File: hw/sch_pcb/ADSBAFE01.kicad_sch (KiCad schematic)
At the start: 66 parts, among them J1 HEADER_2x02_PARALLEL, J2 HEADER_2x12_PARALLEL, J3 MCX 6GHz 50R, M1 HOLE, M2 HOLE, M3 HOLE, M4 HOLE, M5 RFShield_TwoPieces, SW1 SN74LVC1G3157, SW2 SN74LVC1G3157, U1 BGA2818, U2 AD8313xRM, U3 TLV3542, U4 MCP4017-104E 100k, U5 MCP6566, X1 SF2321D

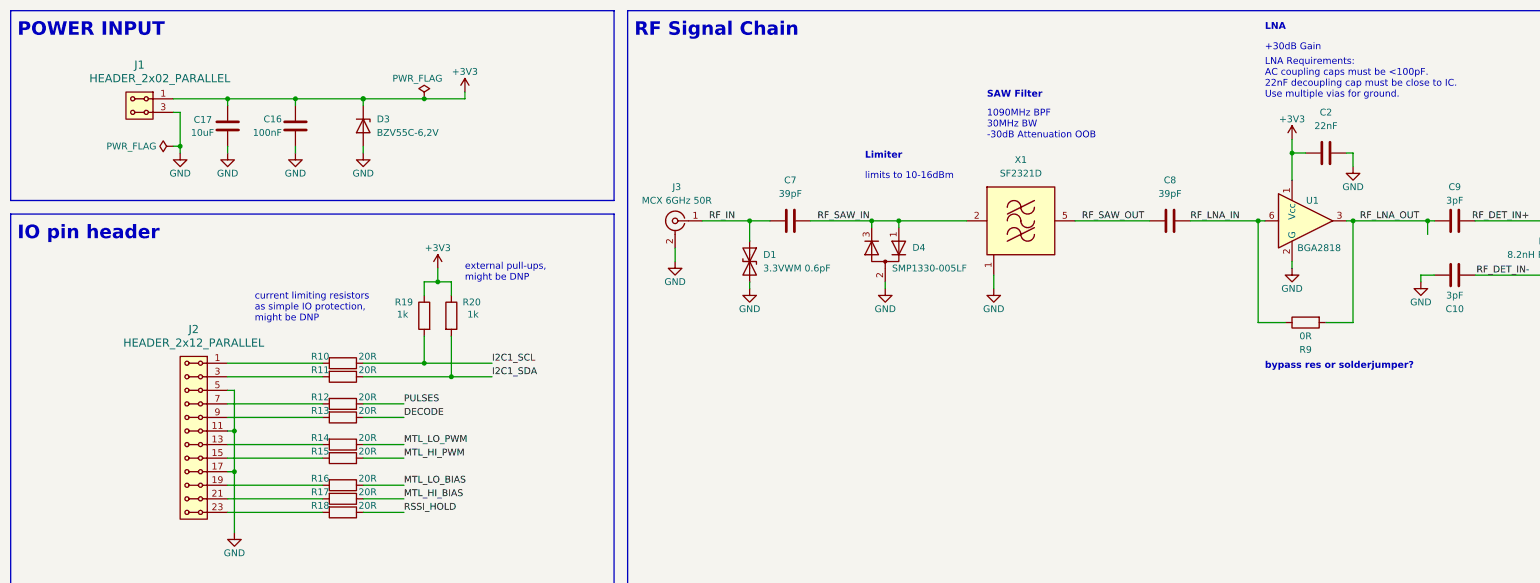
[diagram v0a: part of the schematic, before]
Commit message: first draft of layout
Parts placement viable. Traces sketched only to test whether connections
are viable.
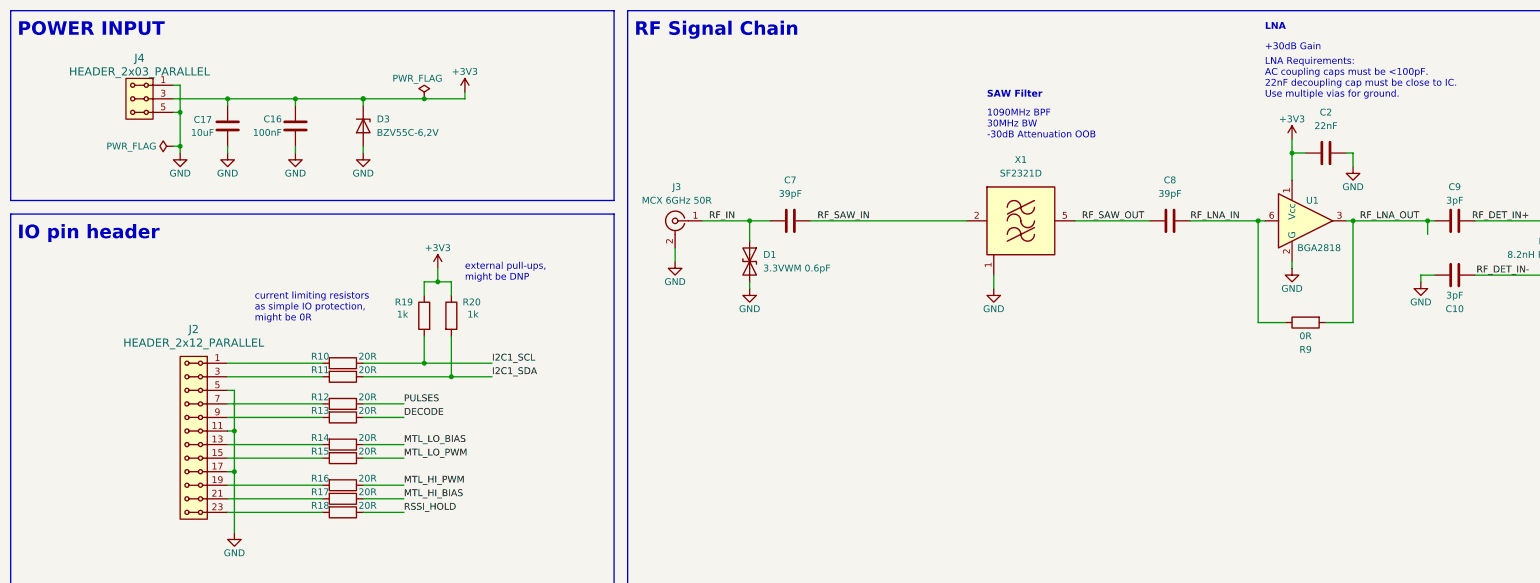
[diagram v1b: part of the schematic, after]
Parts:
- removed D4: SMP1330-005LF, Package_TO_SOT_SMD:SOT-23_Handsoldering, symbol Device:D_Dual_Series_ACK_Parallel
- removed J1: HEADER_2x02_PARALLEL, Mlab_Pin_Headers:Straight_2x02, symbol MLAB_HEADER:HEADER_2x02_PARALLEL
- added J4: HEADER_2x03_PARALLEL, Mlab_Pin_Headers:Straight_2x03, symbol MLAB_HEADER:HEADER_2x03_PARALLEL
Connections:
- net +3V3: now also J4.3, J4.4
- net GND: now also J4.1, J4.2, J4.5, J4.6
- net MTL_HI_PWM: now also R16.1; no longer R15.1
- net MTL_LO_BIAS: now also R14.1; no longer R16.1
- net MTL_LO_PWM: now also R15.1; no longer R14.1
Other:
- note added: "current limiting resistors as simple IO protection, might be 0R"
- note removed: "Limiter"
- note removed: "bypass res or solderjumper?"
- note removed: "current limiting resistors as simple IO protection, might be DNP"
- note removed: "limits to 10-16dBm"

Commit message: Layout done, silk WIP
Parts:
- removed TP1, TP4, TP6, TP7, TP8: TestPoint, TestPoint:TestPoint_Pad_D1.0mm, symbol Connector:TestPoint
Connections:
- net GND: now also J2.19, J2.20; no longer J2.17, J2.18
- net at J2.10, J2.9: now also R17.2; no longer R13.2
- net at J2.23, J2.24: now also R11.2; no longer R18.2
- net at J2.7, J2.8: now also R16.2; no longer R12.2
- net at J2.1, J2.2: now also R14.2; no longer R10.2
- net at J2.15, J2.16: now also R13.2; no longer R15.2
- net at J2.21, J2.22: now also R10.2; no longer R17.2
- net at J2.13, J2.14: now also R12.2; no longer R14.2
- net at J2.3, J2.4: now also R15.2; no longer R11.2
- new net: J2.17, J2.18, R18.2
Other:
- moved on the sheet: J2, R10, R11, R12, R13, R14, R15, R16, R17, R18, R19, R20

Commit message: changed footprint U3, silk started
Footprint of U3 changed to edited version which suits clearence 0,2mm.
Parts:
- U3: footprint Package_SO:VSSOP-8_3x3mm_P0.65mm -> ADSB_project_footprints:VSSOP-8_3x3mm_P0.65mm_small
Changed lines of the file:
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@@
 			)
 		)
-		(property "Footprint" "Package_SO:VSSOP-8_3x3mm_P0.65mm"
+		(property "Footprint" "ADSB_project_footprints:VSSOP-8_3x3mm_P0.65mm_small"
 			(at 77.47 248.92 0)
 			(effects
@@
 			)
 		)
-		(property "Footprint" "Package_SO:VSSOP-8_3x3mm_P0.65mm"
+		(property "Footprint" "ADSB_project_footprints:VSSOP-8_3x3mm_P0.65mm_small"
 			(at 377.19 67.31 0)
 			(effects

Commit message: reannotated, added 3d model of SAW
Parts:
- renumbered C17 to C1, C8 to C10, C2 to C11, C9 to C12, C10 to C13, C3 to C14, C4 to C15, C13 to C16, C6 to C17, C1 to C2, C11 to C3, C16 to C4, C14 to C6, C12 to C7, C15 to C8, C7 to C9, D3 to D1, D1 to D3, J2 to J1, J4 to J2, M5 to M1, M1 to M2, M2 to M3, M3 to M4, M4 to M5, R19 to R12, R20 to R13, R8 to R14, R6 to R15, R9 to R16, R2 to R17, R3 to R18, R5 to R19, R4 to R2, R7 to R20, R14 to R3, R15 to R4, R16 to R5, R17 to R6, R12 to R7, R13 to R8, R18 to R9, TP5 to TP1, U3 to U1, U5 to U2, U1 to U3, U2 to U4, U4 to U5

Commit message: symbols properties cleanup, final checks OK
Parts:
- C10, C9: MPN C106223 -> CC0402JRNPO9BN390; OEM PN CC0402JRNPO9BN390 -> (none); Standard Cost 0.01 -> (none)
- C11, C8: MPN C107026 -> CC0402KRX7R9BB223; OEM PN CC0402KRX7R9BB223 -> (none); Standard Cost 0.01 -> (none)
- C12, C13: MPN C1855211 -> CQ0402CRNPO9BN3R0; OEM PN CQ0402CRNPO9BN3R0 -> (none); Standard Cost 0.01 -> (none)
- C14, C15, C16, C17, C2, C3, C5, C6, C7: MPN C60474 -> CC0402KRX7R7BB104; OEM PN CC0402KRX7R7BB104 -> (none); Standard Cost 0.01 -> (none)
- D2: MPN C82288 -> PMEG2010ER,115; OEM PN PMEG2010ER,115 -> (none); Standard Cost 0.06 -> (none)
- D3: MPN C2912559 -> ESD7351XV2T1G; Note Substituted with TECH PUBLIC dupe due to no stock of onsemi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 -> (none); OEM PN ESD7351XV2T1G -> (none); Standard Cost 0.07 -> (none)
- J3: MPN C88374 -> U.FL-R-SMT-1(80); Note (80) suffix denotes reel size, can be substituted. -> (none); OEM PN U.FL-R-SMT-1(80) -> (none); Standard Cost 0.41 -> (none)
- L1: MPN C361505 -> 0402HP-8N2XJRW; Note Looking for a wire wound inductor with similar performance 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 -> (none); OEM PN SDWL1005C8N2JSTF -> (none); Standard Cost 0.03 -> (none)
- R1, R10, R11, R2, R3, R4, R5, R6, R7, R8, R9: MPN C60490 -> RC0402FR-0710KL; OEM PN RC0402FR-0710KL -> (none); Standard Cost 0.01 -> (none)
- R12, R13, R15, R20: MPN C106235 -> RC0402FR-071KL; OEM PN RC0402FR-071KL -> (none); Standard Cost 0.01 -> (none)
- R14: MPN C138031 -> RC0402FR-0720RL; OEM PN RC0402FR-0720RL -> (none); Standard Cost 0.01 -> (none)
- R16, R19: MPN C60485 -> RC0402JR-070RL; OEM PN RC0402JR-070RL -> (none); Standard Cost 0.01 -> (none)
- R17, R18: MPN C138066 -> RC0402FR-0710RL; OEM PN RC0402FR-0710RL -> (none); Standard Cost 0.01 -> (none)
- SW1, SW2: MPN C38663 -> SN74LVC1G3157DCKR; OEM PN SN74LVC1G3157DCKR -> (none); Standard Cost 0.07 -> (none)
- U1: MPN C2876465 -> TLV3542IDGKR; OEM PN TLV3542IDGKR -> (none); Standard Cost 0.84 -> (none)
- U2: MPN C623508 -> MCP6566T-E/LT; Note Out of stock at LCSC. -> (none); OEM PN MCP6566T-E/LT -> (none); Standard Cost 0.48 -> (none)
- U3: MPN None -> BGA2818,115; Note Not available from LCSC. -> (none); OEM PN BGA2818,115 -> (none); Standard Cost 0.14 -> (none)
- U4: MPN C481897 -> AD8313ARMZ; OEM PN AD8313ARMZ -> (none); Standard Cost 3.35 -> (none)
- U5: MPN C510890 -> MCP4017T-104E/LT; OEM PN MCP4017T-104E/LT -> (none); Standard Cost 0.54 -> (none)
- X1: MPN C3283372 -> SF2321D; Note Out of stock at LCSC. -> (none); OEM PN SF2321D -> (none); Standard Cost 1.10 -> (none)

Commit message: Layout improvements.
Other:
- note removed: "current limiting resistors as simple IO protection, might be 0R"
- company: (none) -> Mlab.cz
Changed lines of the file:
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@@
 		(title "ADSBAFE01A")
 		(date "2026-02-08")
+		(company "Mlab.cz")
+		(comment 1 "Analog RF front-end for 1090 MHz\\nADS-B/Mode-S reception, designed to\\ninterface with MCU module. ")
 	)
 	(rectangle
@@
 		)
 	)
-	(text "current limiting resistors\nas simple IO protection,\nmight be 0R"
-		(exclude_from_sim no)
-		(at 54.61 73.66 0)
-		(effects
-			(font
-				(size 1.27 1.27)
-			)
-			(justify left bottom)
-		)
-	)

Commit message: Move footprints to standard MLAB libraries.
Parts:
- U1: footprint ADSB_project_footprints:VSSOP-8_3x3mm_P0.65mm_small -> Package_SO:VSSOP-8_3x3mm_P0.65mm
- X1: footprint ADSB_project_footprints:Filter_SAW-6_3.8x3.8mm -> MLAB_SAW:Filter_SAW-6_3.8x3.8mm
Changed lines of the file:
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@@
 			)
 		)
-		(property "Footprint" "ADSB_project_footprints:VSSOP-8_3x3mm_P0.65mm_small"
+		(property "Footprint" "Package_SO:VSSOP-8_3x3mm_P0.65mm"
 			(at 77.47 248.92 0)
 			(effects
@@
 			)
 		)
+		(property "UST_ID" ""
+			(at 73.66 242.57 0)
+			(effects
+				(font
+					(size 1.27 1.27)
+				)
+				(hide yes)
+			)
+		)
 		(pin "1"
 		)
@@
 			)
 		)
-		(property "Footprint" "ADSB_project_footprints:Filter_SAW-6_3.8x3.8mm"
+		(property "Footprint" "MLAB_SAW:Filter_SAW-6_3.8x3.8mm"
 			(at 204.47 45.72 0)
 			(effects
@@
 			)
 		)
+		(property "UST_ID" ""
+			(at 204.47 54.61 0)
+			(effects
+				(font
+					(size 1.27 1.27)
+				)
+				(hide yes)
+			)
+		)
 		(pin "1"
 		)
@@
 			)
 		)
-		(property "Footprint" "ADSB_project_footprints:VSSOP-8_3x3mm_P0.65mm_small"
+		(property "Footprint" "Package_SO:VSSOP-8_3x3mm_P0.65mm"
 			(at 377.19 67.31 0)
 			(effects
@@
 			(at 373.38 60.96 0)
 			(effects
+				(font
+					(size 1.27 1.27)
+				)
+				(hide yes)
+			)
+		)
+		(property "UST_ID" ""
+			(at 373.38 60.96 0)
+			(effects
